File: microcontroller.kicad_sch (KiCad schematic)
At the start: 28 parts, among them J2 BOOT0, J3 BOOT1, J4 SWD, SW1 RESET, U4 MAX6369, U5 STM32F103C8Tx, Y1 8MHz

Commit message: capacitor footprints
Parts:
- C10, C11, C13, C14, C15, C16, C17, C18: footprint (none) -> Capacitor_SMD:C_0603_1608Metric
- C12: footprint (none) -> Capacitor_SMD:C_0805_2012Metric
- D5: footprint (none) -> Diode_SMD:D_0603_1608Metric
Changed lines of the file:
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@@
 			)
 		)
-		(property "Footprint" ""
+		(property "Footprint" "Capacitor_SMD:C_0603_1608Metric"
 			(at 112.7252 68.58 0)
 			(effects
@@
 			)
 		)
-		(property "Footprint" ""
+		(property "Footprint" "Capacitor_SMD:C_0603_1608Metric"
 			(at 163.5252 49.53 0)
 			(effects
@@
 			)
 		)
-		(property "Footprint" ""
+		(property "Footprint" "Capacitor_SMD:C_0603_1608Metric"
 			(at 152.0952 49.53 0)
 			(effects
@@
 			)
 		)
-		(property "Footprint" ""
+		(property "Footprint" "Capacitor_SMD:C_0805_2012Metric"
 			(at 140.6652 49.53 0)
 			(effects
@@
 			)
 		)
-		(property "Footprint" ""
+		(property "Footprint" "Capacitor_SMD:C_0603_1608Metric"
 			(at 186.3852 49.53 0)
 			(effects
@@
 			)
 		)
-		(property "Footprint" ""
+		(property "Footprint" "Capacitor_SMD:C_0603_1608Metric"
 			(at 174.9552 49.53 0)
 			(effects
@@
 			)
 		)
-		(property "Footprint" ""
+		(property "Footprint" "Diode_SMD:D_0603_1608Metric"
 			(at 86.36 93.98 0)
 			(effects
@@
 			)
 		)
-		(property "Footprint" ""
+		(property "Footprint" "Capacitor_SMD:C_0603_1608Metric"
 			(at 143.51 74.6252 0)
 			(effects
@@
 			)
 		)
-		(property "Footprint" ""
+		(property "Footprint" "Capacitor_SMD:C_0603_1608Metric"
 			(at 151.13 65.0748 0)
 			(effects
@@
 			)
 		)
-		(property "Footprint" ""
+		(property "Footprint" "Capacitor_SMD:C_0603_1608Metric"
 			(at 40.3352 29.21 0)
 			(effects

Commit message: add more footprints
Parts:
- R23, R24, R25, R26, R27, R28, R29, R30, R31, R32: footprint (none) -> Resistor_SMD:R_0603_1608Metric
- SW1: footprint (none) -> Button_Switch_SMD:SW_SPST_Omron_B3FS-101xP
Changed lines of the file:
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@@
 			)
 		)
-		(property "Footprint" ""
+		(property "Footprint" "Resistor_SMD:R_0603_1608Metric"
 			(at 68.58 76.708 90)
 			(effects
@@
 			)
 		)
-		(property "Footprint" ""
+		(property "Footprint" "Resistor_SMD:R_0603_1608Metric"
 			(at 29.972 34.29 90)
 			(effects
@@
 			)
 		)
-		(property "Footprint" ""
+		(property "Footprint" "Resistor_SMD:R_0603_1608Metric"
 			(at 122.428 99.06 90)
 			(effects
@@
 			)
 		)
-		(property "Footprint" ""
+		(property "Footprint" "Resistor_SMD:R_0603_1608Metric"
 			(at 122.682 53.34 90)
 			(effects
@@
 			)
 		)
-		(property "Footprint" ""
+		(property "Footprint" "Resistor_SMD:R_0603_1608Metric"
 			(at 34.29 76.708 90)
 			(effects
@@
 			)
 		)
-		(property "Footprint" ""
+		(property "Footprint" "Button_Switch_SMD:SW_SPST_Omron_B3FS-101xP"
 			(at 129.54 64.77 0)
 			(effects
@@
 			)
 		)
-		(property "Footprint" ""
+		(property "Footprint" "Resistor_SMD:R_0603_1608Metric"
 			(at 123.952 97.79 90)
 			(effects
@@
 			)
 		)
-		(property "Footprint" ""
+		(property "Footprint" "Resistor_SMD:R_0603_1608Metric"
 			(at 95.758 109.22 90)
 			(effects
@@
 			)
 		)
-		(property "Footprint" ""
+		(property "Footprint" "Resistor_SMD:R_0603_1608Metric"
 			(at 84.582 86.36 90)
 			(effects
@@
 			)
 		)
-		(property "Footprint" ""
+		(property "Footprint" "Resistor_SMD:R_0603_1608Metric"
 			(at 97.282 107.95 90)
 			(effects
@@
 			)
 		)
-		(property "Footprint" ""
+		(property "Footprint" "Resistor_SMD:R_0603_1608Metric"
 			(at 167.132 69.85 90)
 			(effects

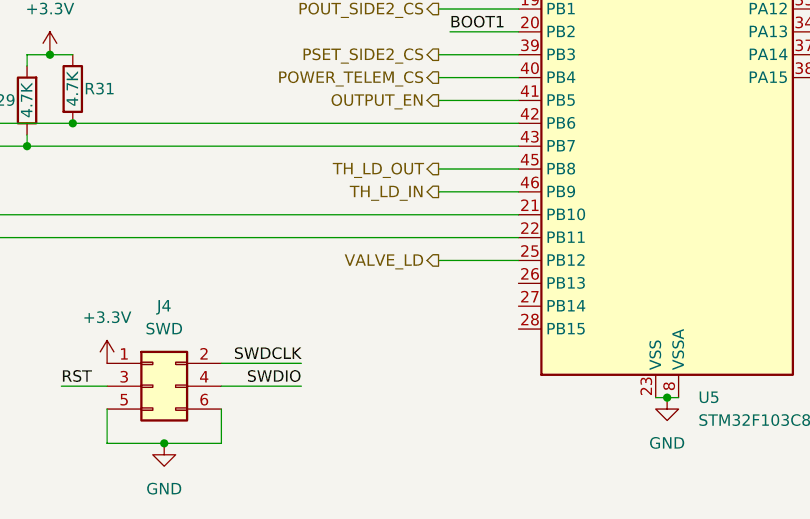
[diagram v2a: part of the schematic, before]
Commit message: ocp reset connect and esd protection
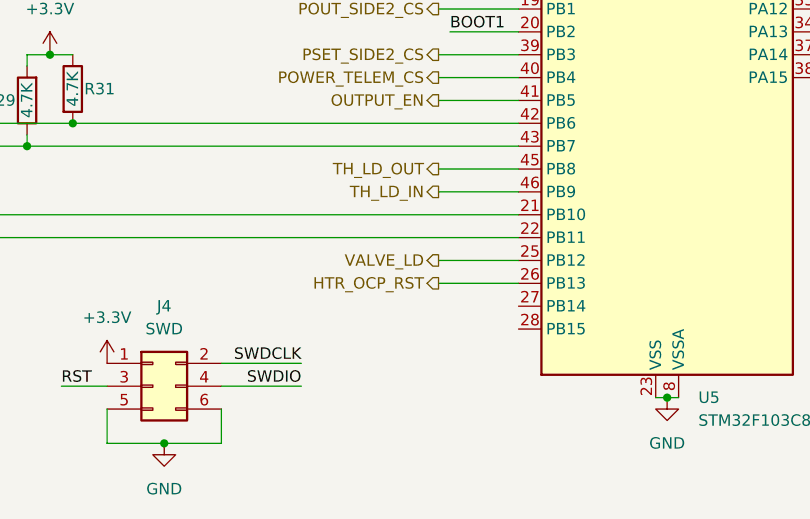
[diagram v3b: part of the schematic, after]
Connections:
- net HTR_OCP_RST: now reaches U5.26 (PB13)
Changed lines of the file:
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@@
+	(wire
+		(pts
+			(xy 166.37 119.38) (xy 175.26 119.38)
+		)
+		(stroke
+			(width 0)
+			(type default)
+		)
+	)
 	(wire
 		(pts
@@
 		)
 	)
+	(hierarchical_label "HTR_OCP_RST"
+		(shape output)
+		(at 166.37 119.38 180)
+		(fields_autoplaced yes)
+		(effects
+			(font
+				(size 1.27 1.27)
+			)
+			(justify right)
+		)
+	)

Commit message: footprint selection
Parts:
- removed J2: BOOT0, symbol Connector:Conn_01x03_Pin
- removed J3: BOOT1, symbol Connector:Conn_01x03_Pin
- removed Y1: 8MHz, symbol Device:Crystal
- added J2: BOOT, Connector_PinHeader_2.54mm:PinHeader_2x03_P2.54mm_Vertical_SMD, symbol Connector_Generic:Conn_02x03_Odd_Even
- added Y1: 8MHz, femta-control:XTAL_ECS-80-12-33Q, symbol Device:Crystal_GND24
- JP2: footprint (none) -> Jumper:SolderJumper-2_P1.3mm_Open_RoundedPad1.0x1.5mm
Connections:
- net +3.3V: now also J2.1 (Pin_1), J2.2 (Pin_2)
- net GND: now also J2.5 (Pin_5), J2.6 (Pin_6), Y1.2, Y1.4
- net at R25.1: now also J2.4 (Pin_4)
- net at C13.2, R32.1, U5.5 (PD0): now also Y1.1
- net at C14.1, R32.2, U5.6 (PD1): now also Y1.3
- net at R24.2: now also J2.3 (Pin_3)
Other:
- note added: "Select a 12-15pF CL Crystal Refer to STM AN2867 for details on osc design"
- moved on the sheet: R24, R25
